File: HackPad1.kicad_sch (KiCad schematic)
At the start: 30 parts, among them J1 Conn_01x04_Pin, SW1 SW_Push, SW10 RotaryEncoder, SW2 SW_Push, SW3 SW_Push, SW4 SW_Push, SW5 SW_Push, SW6 SW_Push, SW7 SW_Push, SW8 SW_Push, SW9 SW_Push, U1 MOUDLE-SEEEDUINO-XIAO

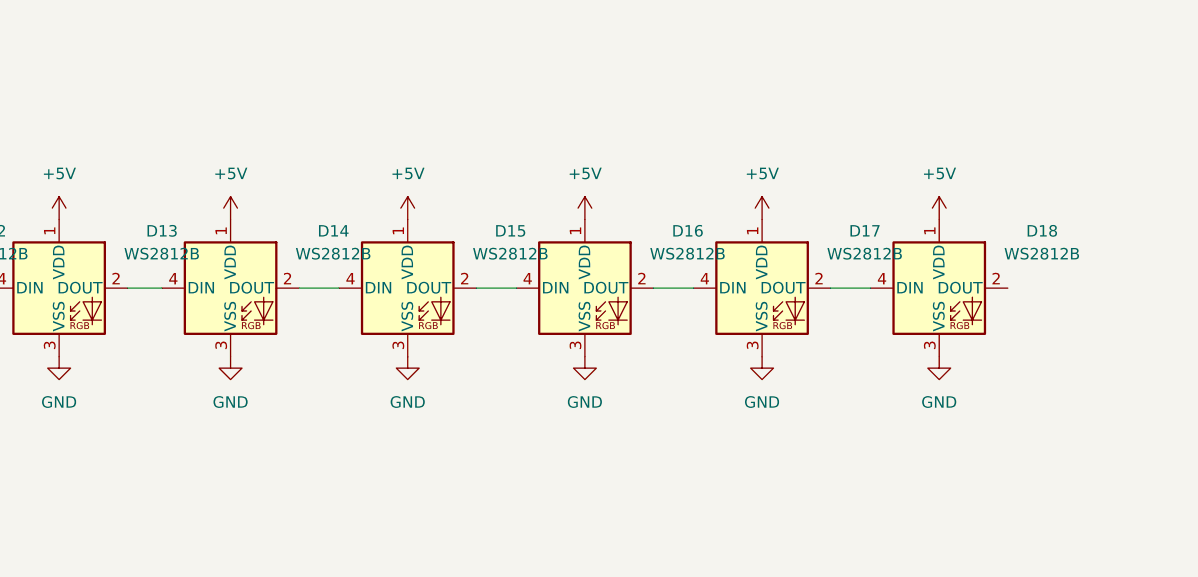
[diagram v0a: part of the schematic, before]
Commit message: updated LED schematic(switched from 9 to 4)
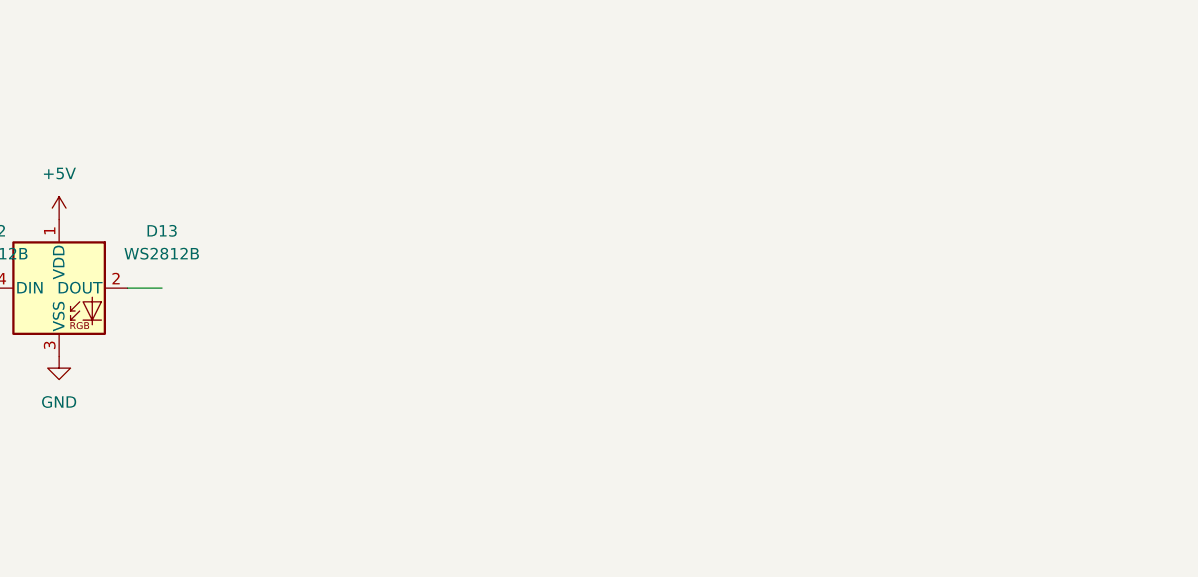
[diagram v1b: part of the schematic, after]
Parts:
- removed D14, D15, D16, D17, D18: WS2812B, Keyboard_Parts:MX_SK6812MINI-E, symbol LED:WS2812B

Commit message: completed pcb design
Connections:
- no-connect marks 0 -> 1
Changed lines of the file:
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@@
 	)
 	(junction
+		(at 88.265 53.975)
+		(diameter 0)
+		(color 0 0 0 0)
+	)
+	(junction
 		(at 185.42 71.12)
 		(diameter 0)
@@
 	)
 	(junction
+		(at 94.615 53.34)
+		(diameter 0)
+		(color 0 0 0 0)
+	)
+	(junction
 		(at 158.75 52.07)
 		(diameter 0)
@@
 	)
 	(junction
+		(at 90.805 46.355)
+		(diameter 0)
+		(color 0 0 0 0)
+	)
+	(junction
 		(at 185.42 52.07)
 		(diameter 0)
 		(color 0 0 0 0)
 	)
+	(no_connect
+		(at 100.33 132.08)
+	)
 	(wire
 		(pts
@@
 	(wire
 		(pts
+			(xy 94.615 53.34) (xy 97.79 53.34)
+		)
+		(stroke
+			(width 0)
+			(type default)
+		)
+	)
+	(wire
+		(pts
 			(xy 96.52 132.08) (xy 100.33 132.08)
 		)
@@
 	(wire
 		(pts
+			(xy 81.915 53.975) (xy 88.265 53.975)
+		)
+		(stroke
+			(width 0)
+			(type default)
+		)
+	)
+	(wire
+		(pts
 			(xy 25.4 73.66) (xy 26.67 73.66)
 		)
@@
 	(wire
 		(pts
+			(xy 90.805 46.355) (xy 94.615 46.355)
+		)
+		(stroke
+			(width 0)
+			(type default)
+		)
+	)
+	(wire
+		(pts
 			(xy 95.25 71.12) (xy 95.25 68.58)
 		)
@@
 	)
 	(symbol
+		(lib_id "power:PWR_FLAG")
+		(at 94.615 46.355 0)
+		(unit 1)
+		(exclude_from_sim no)
+		(in_bom yes)
+		(on_board yes)
+		(dnp no)
+		(fields_autoplaced yes)
+		(property "Reference" "#FLG3"
+			(at 94.615 44.45 0)
+			(effects
+				(font
+					(size 1.27 1.27)
+				)
+				(hide yes)
+			)
+		)
+		(property "Value" "PWR_FLAG"
+			(at 94.615 41.275 0)
+			(effects
+				(font
+					(size 1.27 1.27)
+				)
+			)
+		)
+		(property "Footprint" ""
+			(at 94.615 46.355 0)
+			(effects
+				(font
+					(size 1.27 1.27)
+				)
+				(hide yes)
+			)
+		)
+		(property "Datasheet" "~"
+			(at 94.615 46.355 0)
+			(effects
+				(font
+					(size 1.27 1.27)
+				)
+				(hide yes)
+			)
+		)
+		(property "Description" "Special symbol for telling ERC where power comes from"
+			(at 94.615 46.355 0)
+			(effects
+				(font
+					(size 1.27 1.27)
+				)
+				(hide yes)
+			)
+		)
+		(pin "1"
+		)
+		(instances
+			(project ""
+				(path "/add5448a-8892-4b13-b743-9e2899f953df"
+					(reference "#FLG3")
+					(unit 1)
+				)
+			)
+		)
+	)
+	(symbol
 		(lib_id "Switch:SW_Push")
 		(at 142.24 90.17 0)
@@
 	)
 	(symbol
+		(lib_id "power:PWR_FLAG")
+		(at 97.79 53.34 0)
+		(unit 1)
+		(exclude_from_sim no)
+		(in_bom yes)
+		(on_board yes)
+		(dnp no)
+		(fields_autoplaced yes)
+		(property "Reference" "#FLG2"
+			(at 97.79 51.435 0)
+			(effects
+				(font
+					(size 1.27 1.27)
+				)
+				(hide yes)
+			)
+		)
+		(property "Value" "PWR_FLAG"
+			(at 97.79 48.895 0)
+			(effects
+				(font
+					(size 1.27 1.27)
+				)
+			)
+		)
+		(property "Footprint" ""
+			(at 97.79 53.34 0)
+			(effects
+				(font
+					(size 1.27 1.27)
+				)
+				(hide yes)
+			)
+		)
+		(property "Datasheet" "~"
+			(at 97.79 53.34 0)
+			(effects
+				(font
+					(size 1.27 1.27)
+				)
+				(hide yes)
+			)
+		)
+		(property "Description" "Special symbol for telling ERC where power comes from"
+			(at 97.79 53.34 0)
+			(effects
+				(font
+					(size 1.27 1.27)
+				)
+				(hide yes)
+			)
+		)
+		(pin "1"
+		)
+		(instances
+			(project ""
+				(path "/add5448a-8892-4b13-b743-9e2899f953df"
+					(reference "#FLG2")
+					(unit 1)
+				)
+			)
+		)
+	)
+	(symbol
 		(lib_id "Device:D")
 		(at 154.94 90.17 180)
@@
 					(unit 1)
 				)
+			)
+		)
+	)
+	(symbol
+		(lib_id "power:PWR_FLAG")
+		(at 81.915 53.975 0)
+		(unit 1)
+		(exclude_from_sim no)
+		(in_bom yes)
+		(on_board yes)
+		(dnp no)
+		(fields_autoplaced yes)
+		(property "Reference" "#FLG1"
+			(at 81.915 52.07 0)
+			(effects
+				(font
+					(size 1.27 1.27)
+				)
+				(hide yes)
+			)
+		)
+		(property "Value" "PWR_FLAG"
+			(at 81.915 49.53 0)
+			(effects
+				(font
+					(size 1.27 1.27)
+				)
+			)
+		)
+		(property "Footprint" ""
+			(at 81.915 53.975 0)
+			(effects
+				(font
+					(size 1.27 1.27)
+				)
+				(hide yes)
+			)
+		)
+		(property "Datasheet" "~"
+			(at 81.915 53.975 0)
+			(effects
+				(font
+					(size 1.27 1.27)
+				)
+				(hide yes)
+			)
+		)
+		(property "Description" "Special symbol for telling ERC where power comes from"
+			(at 81.915 53.975 0)
+			(effects
+				(font
+					(size 1.27 1.27)
+				)
+				(hide yes)
+			)
+		)
+		(pin "1"
+		)
+		(instances
+			(project ""
+				(path "/add5448a-8892-4b13-b743-9e2899f953df"
+					(reference "#FLG1")
+					(unit 1)
+				)
